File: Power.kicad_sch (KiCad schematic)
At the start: 3 parts, among them U3 MAX17501AxTB

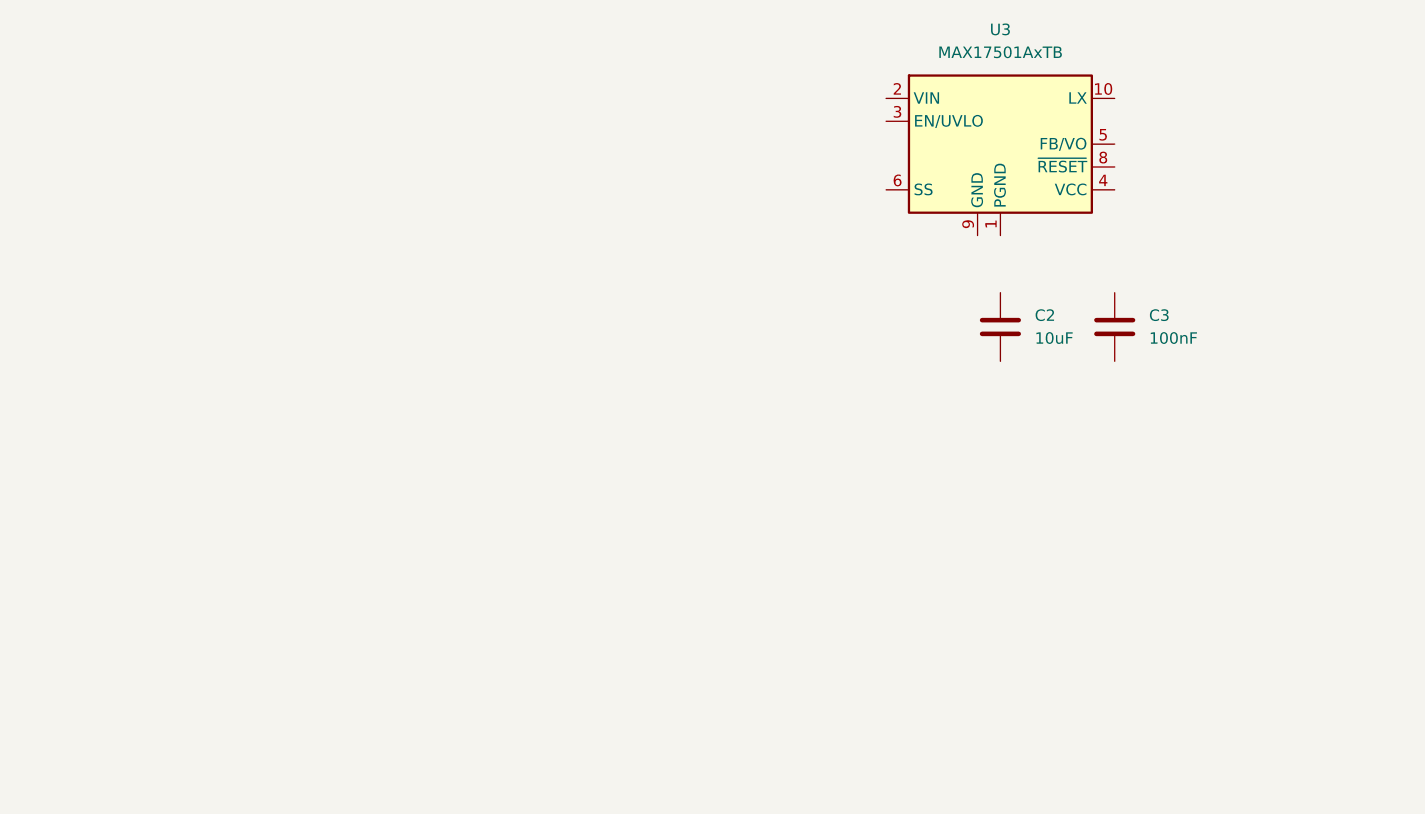
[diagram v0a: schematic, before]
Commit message: Concluded ESP32 + Power
still need to have a look around for errors
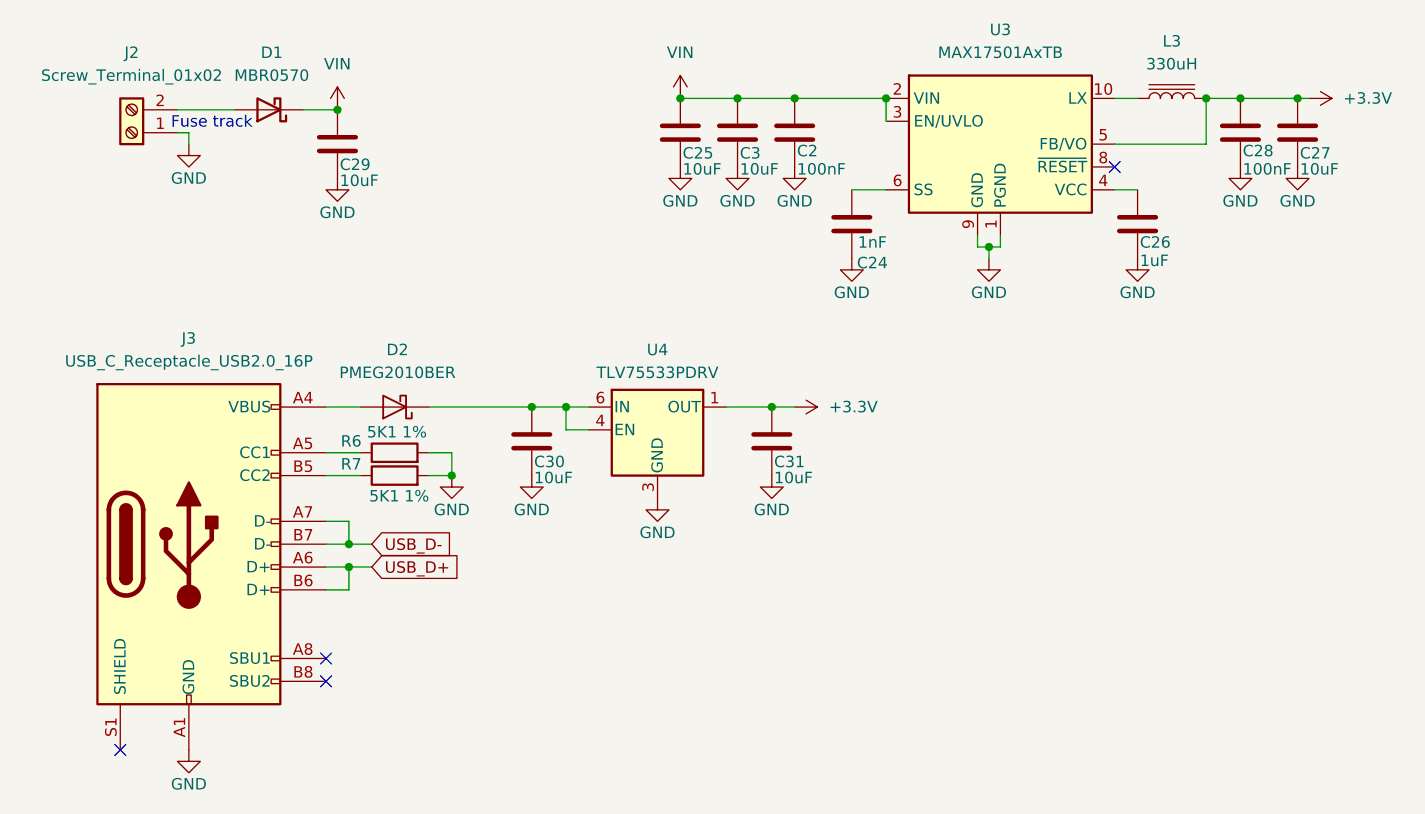
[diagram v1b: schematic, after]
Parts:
- added C24: 1nF, RevK:C_0603, symbol Device:C
- added C25, C27, C29, C30, C31: 10uF, Capacitor_SMD:C_0805_2012Metric, symbol Device:C
- added C26: 1uF, Capacitor_SMD:C_0603_1608Metric, symbol Device:C
- added C28: 100nF, Capacitor_SMD:C_0603_1608Metric, symbol Device:C
- added D1: MBR0570, Fuse:Fuseholder_Littelfuse_Nano2_157x, symbol Diode:MBR0570
- added D2: PMEG2010BER, Diode_SMD:Nexperia_CFP3_SOD-123W, symbol Diode:PMEG2010BER
- added J2: Screw_Terminal_01x02, TerminalBlock_Phoenix:TerminalBlock_Phoenix_MPT-0,5-2-2.54_1x02_P2.54mm_Horizontal, symbol Connector:Screw_Terminal_01x02
- added J3: USB_C_Receptacle_USB2.0_16P, Connector_USB:USB_C_Receptacle_GCT_USB4110, symbol Connector:USB_C_Receptacle_USB2.0_16P
- added L3: 330uH, Inductor_SMD:L_Bourns_SRN6045TA, symbol Device:L_Iron
- added R6, R7: 5K1 1%, RevK:R_0603, symbol Device:R
- added U4: TLV75533PDRV, Package_DIP:DIP-8-16_W7.62mm_Socket_LongPads, symbol Regulator_Linear:TLV75533PDRV
- C2: value 10uF -> 100nF; footprint Capacitor_SMD:C_0805_2012Metric -> Capacitor_SMD:C_0603_1608Metric
- C3: value 100nF -> 10uF; footprint Capacitor_SMD:C_0603_1608Metric -> Capacitor_SMD:C_0805_2012Metric
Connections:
- net GND: now reaches U3.1 (PGND)
- net GND: now also C2.1, C3.2, U3.11 (GND), U3.9 (GND), C24.1, C25.2, C26.1, C27.2, C28.1, C29.2, C30.2, C31.2, J2.1 (Pin_1), J3.A1 (GND), J3.A12 (GND), J3.B1 (GND), J3.B12 (GND), R6.2, R7.2, U4.3 (GND), U4.7 (GND)
- net at U3.10 (LX): now also L3.1
- net VIN: now reaches U3.2 (VIN)
- net VIN: now also C2.2, C3.1, U3.3 (EN/UVLO), C25.1, C29.1, D1.1 (K)
- net at U3.4 (VCC): now also C26.2
- net +3.3V: now reaches U3.5 (FB/VO)
- net +3.3V: now also C27.1, C28.2, C31.1, L3.2, U4.1 (OUT)
- net at U3.6 (SS): now also C24.2
- new net: C30.1, D2.1 (K), U4.4 (EN), U4.6 (IN)
- new net: J3.A5 (CC1), R6.1
- new net: D1.2 (A), J2.2 (Pin_2)
- new net: D2.2 (A), J3.A4 (VBUS), J3.A9 (VBUS), J3.B4 (VBUS), J3.B9 (VBUS)
- new net: J3.B5 (CC2), R7.1
- new net USB_D+: J3.A6 (D+), J3.B6 (D+)
- new net USB_D-: J3.A7 (D-), J3.B7 (D-)
- no-connect marks 0 -> 4
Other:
- note added: "Fuse track"

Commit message: Added Revs + PDF
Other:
- title: (none) -> Homekey PCB ESP32C3
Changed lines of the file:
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@@
 	(generator_version "8.0")
 	(paper "A4")
+	(title_block
+		(title "Homekey PCB ESP32C3")
+		(date "2024-07-03")
+		(rev "Rev A")
+	)
 	(junction
 		(at 144.78 82.55)

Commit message: Start of layout
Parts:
- C24: footprint RevK:C_0603 -> Capacitor_SMD:C_0603_1608Metric
- R6, R7: footprint RevK:R_0603 -> Resistor_SMD_AKL:R_0603_1608Metric; symbol Device:R -> PCM_Resistor_AKL:R_0603
- U4: footprint Package_DIP:DIP-8-16_W7.62mm_Socket_LongPads -> Package_SON:WSON-6-1EP_2x2mm_P0.65mm_EP1x1.6mm
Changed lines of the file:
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@@
 	)
 	(symbol
-		(lib_id "Device:R")
+		(lib_id "PCM_Resistor_AKL:R_0603")
 		(at 90.17 121.92 90)
 		(unit 1)
@@
 			)
 		)
-		(property "Footprint" "RevK:R_0603"
-			(at 90.17 123.698 90)
+		(property "Footprint" "Resistor_SMD_AKL:R_0603_1608Metric"
+			(at 101.6 121.92 0)
 			(effects
 				(font
@@
 			)
 		)
-		(property "Footprint" "RevK:C_0603"
+		(property "Footprint" "Capacitor_SMD:C_0603_1608Metric"
 			(at 140.0048 92.71 0)
 			(effects
@@
 	)
 	(symbol
-		(lib_id "Device:R")
+		(lib_id "PCM_Resistor_AKL:R_0603")
 		(at 90.17 124.46 90)
 		(unit 1)
@@
 			)
 		)
-		(property "Footprint" "RevK:R_0603"
-			(at 90.17 126.238 90)
+		(property "Footprint" "Resistor_SMD_AKL:R_0603_1608Metric"
+			(at 101.6 124.46 0)
 			(effects
 				(font
@@
 			)
 		)
-		(property "Footprint" "Package_DIP:DIP-8-16_W7.62mm_Socket_LongPads"
+		(property "Footprint" "Package_SON:WSON-6-1EP_2x2mm_P0.65mm_EP1x1.6mm"
 			(at 119.38 111.125 0)
 			(effects

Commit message: Finished rev A PCB V 0.1
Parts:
- removed C29: 10uF, Capacitor_SMD:C_0805_2012Metric, symbol Device:C
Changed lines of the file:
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@@
-	)
-	(junction
-		(at 83.82 83.82)
-		(diameter 0)
-		(color 0 0 0 0)
 	)
 	(junction
@@
 	(symbol
 		(lib_id "power:GND")
-		(at 83.82 91.44 0)
-		(unit 1)
-		(exclude_from_sim no)
-		(in_bom yes)
-		(on_board yes)
-		(dnp no)
-		(property "Reference" "#PWR033"
-			(at 83.82 97.79 0)
-			(effects
-				(font
-					(size 1.27 1.27)
-				)
-				(hide yes)
-			)
-		)
-		(property "Value" "GND"
-			(at 83.82 95.25 0)
-			(effects
-				(font
-					(size 1.27 1.27)
-				)
-			)
-		)
-		(property "Footprint" ""
-			(at 83.82 91.44 0)
-			(effects
-				(font
-					(size 1.27 1.27)
-				)
-				(hide yes)
-			)
-		)
-		(property "Datasheet" ""
-			(at 83.82 91.44 0)
-			(effects
-				(font
-					(size 1.27 1.27)
-				)
-				(hide yes)
-			)
-		)
-		(property "Description" "Power symbol creates a global label with name \"GND\" , ground"
-			(at 83.82 91.44 0)
-			(effects
-				(font
-					(size 1.27 1.27)
-				)
-				(hide yes)
-			)
-		)
-		(pin "1"
-		)
-		(instances
-			(project "Homekey"
-				(path "/8ef12b84-4556-413e-8e5a-ce52402aeac0/e280ed20-7e15-4ef2-ac9d-516095406e26"
-					(reference "#PWR033")
-					(unit 1)
-				)
-			)
-		)
-	)
-	(symbol
-		(lib_id "power:GND")
 		(at 67.31 154.94 0)
 		(unit 1)
@@
 					(unit 1)
 				)
-			)
-		)
-	)
-	(symbol
-		(lib_id "Device:C")
-		(at 83.82 87.63 0)
-		(unit 1)
-		(exclude_from_sim no)
-		(in_bom yes)
-		(on_board yes)
-		(dnp no)
-		(property "Reference" "C29"
-			(at 84.074 89.916 0)
-			(effects
-				(font
-					(size 1.27 1.27)
-				)
-				(justify left)
-			)
-		)
-		(property "Value" "10uF"
-			(at 84.074 91.694 0)
-			(effects
-				(font
-					(size 1.27 1.27)
-				)
-				(justify left)
-			)
-		)
-		(property "Footprint" "Capacitor_SMD:C_0805_2012Metric"
-			(at 84.7852 91.44 0)
-			(effects
-				(font
-					(size 1.27 1.27)
-				)
-				(hide yes)
-			)
-		)
-		(property "Datasheet" "~"
-			(at 83.82 87.63 0)
-			(effects
-				(font
-					(size 1.27 1.27)
-				)
-				(hide yes)
-			)
-		)
-		(property "Description" "Unpolarized capacitor"
-			(at 83.82 87.63 0)
-			(effects
-				(font
-					(size 1.27 1.27)
-				)
-				(hide yes)
-			)
-		)
-		(pin "2"
-		)
-		(pin "1"
-		)
-		(instances
-			(project "Homekey"
-				(path "/8ef12b84-4556-413e-8e5a-ce52402aeac0/e280ed20-7e15-4ef2-ac9d-516095406e26"
-					(reference "C29")
-					(unit 1)
-				)

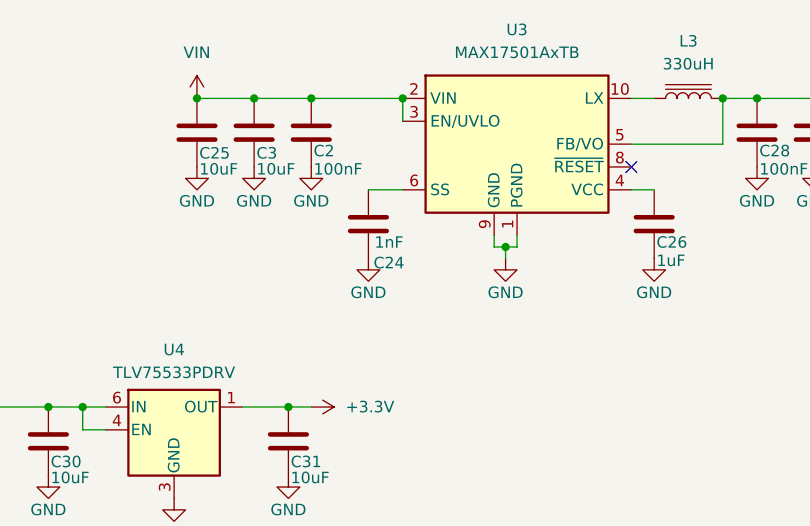
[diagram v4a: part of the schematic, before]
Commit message: Fixed SS problem, bumped C24 to 3300pF
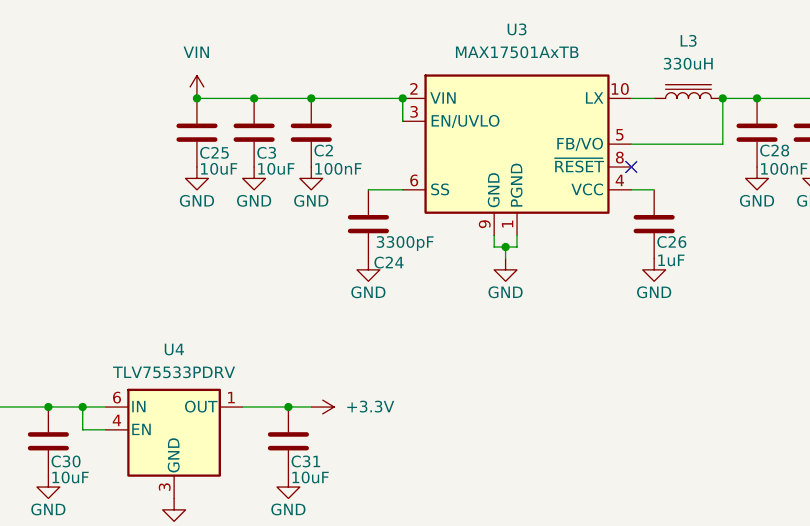
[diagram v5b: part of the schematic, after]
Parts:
- C24: value 1nF -> 3300pF
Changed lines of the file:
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@@
 			)
 		)
-		(property "Value" "1nF"
-			(at 143.256 98.552 0)
+		(property "Value" "3300pF"
+			(at 145.034 98.552 0)
 			(effects
 				(font
